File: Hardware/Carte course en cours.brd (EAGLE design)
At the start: 47 x 28.6 mm, 41 parts, among them J2 AVR_SPI_PROG_3X2NS, J3 PWR IN, J4 RC receiver, J5 ESC, J6 ESC, J7 MICRO-SD_CARD_SOCKET, J8 ESC, U1 LM317, U2 ATMEGA328P_TQFP, U3 FT232RL, U4 MPU6050, Y1 16MHz

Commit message: Changed MCU frequency to 8MHz, to run safe at 3.3V
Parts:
- Y1: value 16MHz -> 8MHz
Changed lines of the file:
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@@
 <attribute name="VALUE" x="13.49375" y="13.335" size="1" layer="27" font="vector" ratio="11" rot="R270" align="bottom-center"/>
 </element>
-<element name="Y1" library="SparkFun-Clocks" library_urn="urn:adsk.eagle:library:511" package="CRYSTAL-SMD-5X3.2-4PAD" package3d_urn="urn:adsk.eagle:package:37518/1" value="16MHz" x="26.035" y="16.51" smashed="yes" rot="MR180">
+<element name="Y1" library="SparkFun-Clocks" package="CRYSTAL-SMD-5X3.2-4PAD" value="8MHz" x="26.035" y="16.51" smashed="yes" rot="MR180">
 <attribute name="NAME" x="24.765" y="14.605" size="1" layer="26" font="vector" ratio="11" rot="MR180" align="bottom-center"/>
-<attribute name="PROD_ID" value="XTAL-08218" x="26.035" y="16.51" size="1.778" layer="28" rot="MR180" display="off"/>
-<attribute name="SF_ID" value="COM-00094" x="26.035" y="16.51" size="1.778" layer="28" rot="MR180" display="off"/>
-<attribute name="VALUE" x="26.035" y="18.415" size="1" layer="28" font="vector" ratio="11" rot="MR180" align="top-center"/>
+<attribute name="PROD_ID" value="XTAL-09431" x="26.035" y="16.51" size="1.778" layer="28" rot="MR180" display="off"/>
+<attribute name="VALUE" value="8MHz" x="26.035" y="18.415" size="1" layer="28" font="vector" ratio="11" rot="MR180" align="top-center"/>
 </element>
 <element name="U1" library="bt_regulator" package="SOT-223-3" value="LM317" x="10.16" y="13.335" smashed="yes" rot="R180">

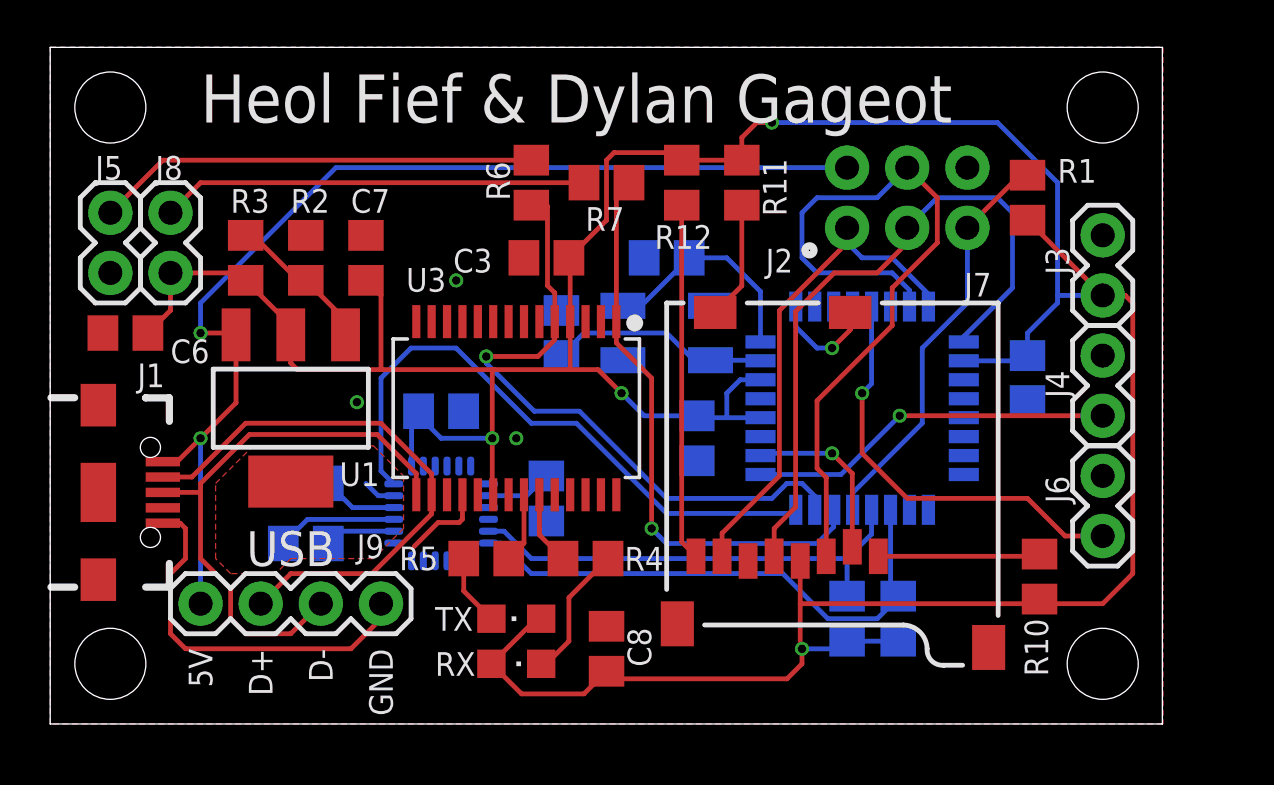
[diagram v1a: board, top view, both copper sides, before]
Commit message: Add 4 GPIO
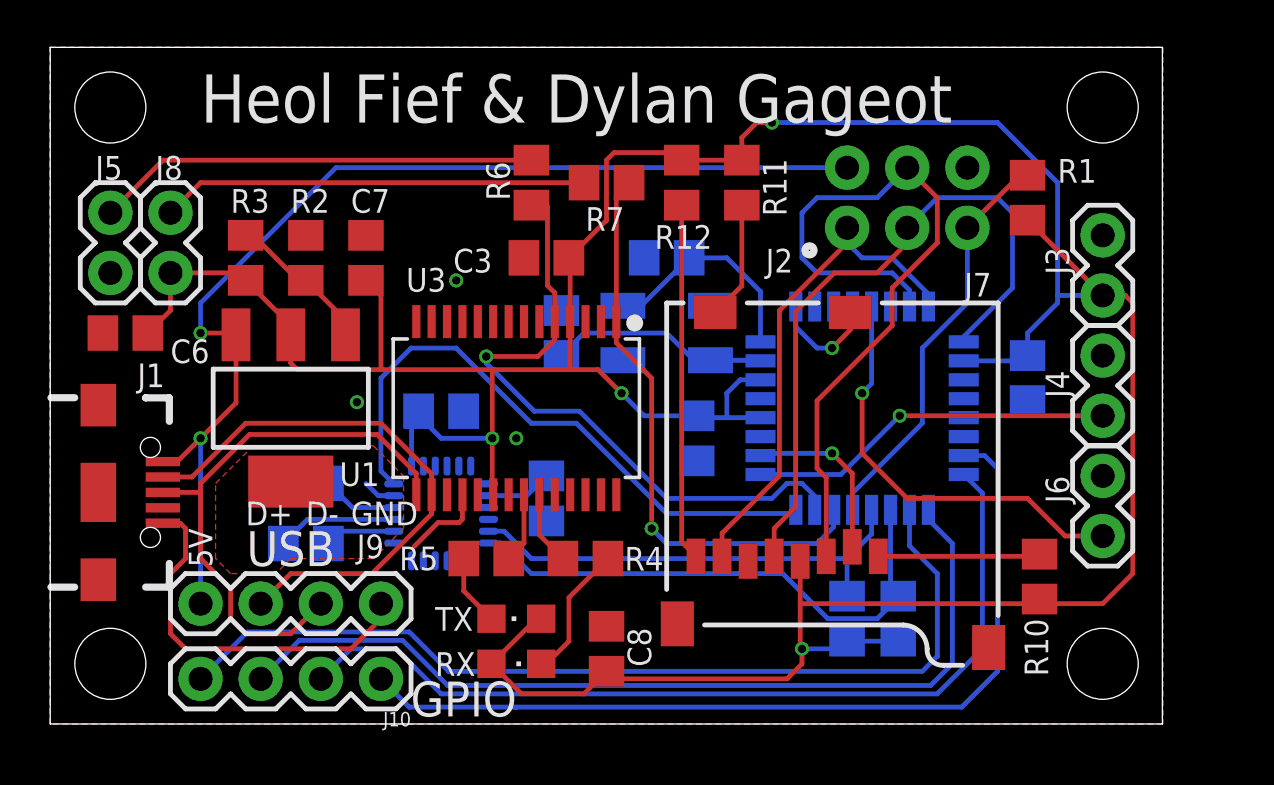
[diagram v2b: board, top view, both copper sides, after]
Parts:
- added J10: GPIO, SparkFun-Connectors:1X04
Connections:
- new net GPIO1: J10.1, U2.23
- new net GPIO2: J10.2, U2.24
- new net GPIO3: J10.3, U2.25
- new net GPIO4: J10.4, U2.26
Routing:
- net GPIO4: track 0.00 -> 39.6 mm
- net GPIO3: track 0.00 -> 38.0 mm
- net GPIO2: track 0.00 -> 37.7 mm
- net GPIO1: track 0.00 -> 37.4 mm
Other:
- board text added: "GPIO"
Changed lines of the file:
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@@
 <?xml version="1.0" encoding="utf-8"?>
 <!DOCTYPE eagle SYSTEM "eagle.dtd">
-<eagle version="8.5.0">
+<eagle version="8.7.0">
 <drawing>
 <settings>
@@
 <layer number="43" name="vRestrict" color="2" fill="10" visible="yes" active="yes"/>
 <layer number="44" name="Drills" color="7" fill="1" visible="no" active="yes"/>
-<layer number="45" name="Holes" color="7" fill="1" visible="yes" active="yes"/>
+<layer number="45" name="Holes" color="7" fill="1" visible="no" active="yes"/>
 <layer number="46" name="Milling" color="3" fill="1" visible="no" active="yes"/>
 <layer number="47" name="Measures" color="7" fill="1" visible="no" active="yes"/>
-<layer number="48" name="Document" color="7" fill="1" visible="no" active="yes"/>
+<layer number="48" name="Document" color="7" fill="1" visible="yes" active="yes"/>
 <layer number="49" name="Reference" color="7" fill="1" visible="yes" active="yes"/>
 <layer number="50" name="dxf" color="7" fill="1" visible="no" active="no"/>
-<layer number="51" name="tDocu" color="7" fill="1" visible="no" active="yes"/>
-<layer number="52" name="bDocu" color="7" fill="1" visible="no" active="yes"/>
+<layer number="51" name="tDocu" color="7" fill="1" visible="yes" active="yes"/>
+<layer number="52" name="bDocu" color="7" fill="1" visible="yes" active="yes"/>
 <layer number="53" name="tGND_GNDA" color="7" fill="9" visible="no" active="no"/>
 <layer number="54" name="bGND_GNDA" color="1" fill="9" visible="no" active="no"/>
@@
 <layer number="134" name="silk_top" color="7" fill="1" visible="no" active="no"/>
 <layer number="135" name="silk_bottom" color="7" fill="1" visible="no" active="no"/>
-<layer number="136" name="silktop" color="7" fill="1" visible="yes" active="yes"/>
-<layer number="137" name="silkbottom" color="7" fill="1" visible="yes" active="yes"/>
+<layer number="136" name="silktop" color="7" fill="1" visible="no" active="yes"/>
+<layer number="137" name="silkbottom" color="7" fill="1" visible="no" active="yes"/>
 <layer number="144" name="Drill_legend" color="7" fill="1" visible="yes" active="yes"/>
-<layer number="145" name="DrillLegend_01-16" color="7" fill="1" visible="yes" active="yes"/>
-<layer number="146" name="DrillLegend_01-20" color="7" fill="1" visible="yes" active="yes"/>
+<layer number="145" name="DrillLegend_01-16" color="7" fill="1" visible="no" active="yes"/>
+<layer number="146" name="DrillLegend_01-20" color="7" fill="1" visible="no" active="yes"/>
 <layer number="150" name="Notes" color="7" fill="1" visible="yes" active="yes"/>
 <layer number="151" name="HeatSink" color="7" fill="1" visible="yes" active="yes"/>
@@
 <layer number="154" name="FabDoc2" color="7" fill="1" visible="yes" active="yes"/>
 <layer number="155" name="FabDoc3" color="7" fill="1" visible="yes" active="yes"/>
-<layer number="166" name="AntennaArea" color="7" fill="1" visible="yes" active="yes"/>
-<layer number="168" name="4mmHeightArea" color="7" fill="1" visible="yes" active="yes"/>
+<layer number="166" name="AntennaArea" color="7" fill="1" visible="no" active="yes"/>
+<layer number="168" name="4mmHeightArea" color="7" fill="1" visible="no" active="yes"/>
 <layer number="199" name="Contour" color="7" fill="1" visible="yes" active="yes"/>
 <layer number="200" name="200bmp" color="1" fill="10" visible="yes" active="yes"/>
@@
 <hole x="44.45" y="26.035" drill="3"/>
 <text x="6.35" y="25.4" size="2.032" layer="25" font="vector" ratio="11" distance="80">Heol Fief &amp; Dylan Gageot</text>
-<text x="6.35" y="3.175" size="1" layer="25" font="vector" ratio="11" rot="R270" align="center-left">5V</text>
-<text x="8.89" y="3.175" size="1" layer="25" font="vector" ratio="11" rot="R270" align="center-left">D+</text>
-<text x="11.43" y="3.175" size="1" layer="25" font="vector" ratio="11" rot="R270" align="center-left">D-</text>
-<text x="13.97" y="3.175" size="1" layer="25" font="vector" ratio="11" rot="R270" align="center-left">GND</text>
+<text x="6.35" y="8.255" size="1" layer="25" font="vector" ratio="11" rot="R270" align="center-left">5V</text>
+<text x="8.255" y="8.89" size="1" layer="25" font="vector" ratio="11" align="center-left">D+</text>
+<text x="10.795" y="8.89" size="1" layer="25" font="vector" ratio="11" align="center-left">D-</text>
+<text x="12.7" y="8.89" size="1" layer="25" font="vector" ratio="11" align="center-left">GND</text>
 <wire x1="15.24" y1="24.3332" x2="19.6511" y2="25.50846875" width="0.3556" layer="22"/>
 <wire x1="19.6511" y1="25.50846875" x2="19.6511" y2="25.92653125" width="0.3556" layer="22" curve="145.292146"/>
@@
 <text x="10.16" y="6.6675" size="1.4732" layer="25" font="vector" ratio="17" distance="1" align="bottom-center">USB</text>
 <circle x="32.0675" y="20.0025" radius="0.1524" width="0.381" layer="21"/>
+<text x="17.4625" y="0.3175" size="1.4732" layer="25" font="vector" ratio="17" distance="1" align="bottom-center">GPIO</text>
 </plain>
 <attributes>
@@
 </element>
 <element name="LOGO1" library="SparkFun-Aesthetics" library_urn="urn:adsk.eagle:library:507" package="OSHW-LOGO-M" package3d_urn="urn:adsk.eagle:package:37126/1" value="OSHW-LOGOM" x="10.16" y="15.24" rot="MR0"/>
+<element name="J10" library="SparkFun-Connectors" library_urn="urn:adsk.eagle:library:513" package="1X04" package3d_urn="urn:adsk.eagle:package:38085/1" value="GPIO" x="13.97" y="1.905" rot="R180">
+<attribute name="PROD_ID" value="CONN-09696" x="13.97" y="1.905" size="1.778" layer="27" rot="R180" display="off"/>
+</element>
 </elements>
 <signals>
@@
 <contactref element="U1" pad="4"/>
 </signal>
+<signal name="GPIO1">
+<contactref element="U2" pad="23"/>
+<contactref element="J10" pad="1"/>
+<wire x1="38.5826" y1="11.335" x2="39.465" y2="11.335" width="0.2032" layer="16"/>
+<wire x1="39.465" y1="11.335" x2="40.005" y2="10.795" width="0.2032" layer="16"/>
+<wire x1="40.005" y1="10.795" x2="40.005" y2="2.2225" width="0.2032" layer="16"/>
+<wire x1="38.4937" y1="0.7112" x2="19.685" y2="0.7112" width="0.2032" layer="16"/>
+<wire x1="19.685" y1="0.7112" x2="19.6088" y2="0.7112" width="0.2032" layer="16"/>
+<wire x1="40.005" y1="2.2225" x2="38.4937" y2="0.7112" width="0.2032" layer="16"/>
+<wire x1="19.6088" y1="0.7112" x2="15.1638" y2="0.7112" width="0.2032" layer="16"/>
+<wire x1="15.1638" y1="0.7112" x2="13.97" y2="1.905" width="0.2032" layer="16"/>
+</signal>
+<signal name="GPIO2">
+<contactref element="U2" pad="24"/>
+<contactref element="J10" pad="2"/>
+<wire x1="38.5826" y1="10.535" x2="39.37" y2="9.7476" width="0.2032" layer="16"/>
+<wire x1="39.37" y1="9.7476" x2="39.37" y2="3.175" width="0.2032" layer="16"/>
+<wire x1="39.37" y1="3.175" x2="37.465" y2="1.27" width="0.2032" layer="16"/>
+<wire x1="16.51" y1="1.27" x2="14.605" y2="3.175" width="0.2032" layer="16"/>
+<wire x1="14.605" y1="3.175" x2="12.7" y2="3.175" width="0.2032" layer="16"/>
+<wire x1="12.7" y1="3.175" x2="11.43" y2="1.905" width="0.2032" layer="16"/>
+<wire x1="37.465" y1="1.27" x2="16.51" y2="1.27" width="0.2032" layer="16"/>
+</signal>
+<signal name="GPIO3">
+<contactref element="U2" pad="25"/>
+<contactref element="J10" pad="3"/>
+<wire x1="37.09" y1="9.0424" x2="37.09" y2="8.63" width="0.2032" layer="16"/>
+<wire x1="37.09" y1="8.63" x2="38.1" y2="7.62" width="0.2032" layer="16"/>
+<wire x1="38.1" y1="7.62" x2="38.1" y2="2.54" width="0.2032" layer="16"/>
+<wire x1="38.1" y1="2.54" x2="37.1856" y2="1.6256" width="0.2032" layer="16"/>
+<wire x1="14.8844" y1="3.5306" x2="10.5156" y2="3.5306" width="0.2032" layer="16"/>
+<wire x1="16.7894" y1="1.6256" x2="14.8844" y2="3.5306" width="0.2032" layer="16"/>
+<wire x1="10.5156" y1="3.5306" x2="8.89" y2="1.905" width="0.2032" layer="16"/>
+<wire x1="37.1856" y1="1.6256" x2="16.7894" y2="1.6256" width="0.2032" layer="16"/>
+</signal>
+<signal name="GPIO4">
+<contactref element="U2" pad="26"/>
+<contactref element="J10" pad="4"/>
+<wire x1="36.29" y1="9.0424" x2="36.29" y2="7.525" width="0.2032" layer="16"/>
+<wire x1="36.29" y1="7.525" x2="37.465" y2="6.35" width="0.2032" layer="16"/>
+<wire x1="37.465" y1="6.35" x2="37.465" y2="2.8575" width="0.2032" layer="16"/>
+<wire x1="37.465" y1="2.8575" x2="36.83" y2="2.2225" width="0.2032" layer="16"/>
+<wire x1="36.83" y1="2.2225" x2="23.495" y2="2.2225" width="0.2032" layer="16"/>
+<wire x1="23.495" y1="2.2225" x2="23.1775" y2="2.2225" width="0.2032" layer="16"/>
+<wire x1="23.1775" y1="2.2225" x2="16.8275" y2="2.2225" width="0.2032" layer="16"/>
+<wire x1="15.1638" y1="3.8862" x2="8.3312" y2="3.8862" width="0.2032" layer="16"/>
+<wire x1="16.8275" y1="2.2225" x2="15.1638" y2="3.8862" width="0.2032" layer="16"/>
+<wire x1="8.3312" y1="3.8862" x2="6.35" y2="1.905" width="0.2032" layer="16"/>
+</signal>
 </signals>
